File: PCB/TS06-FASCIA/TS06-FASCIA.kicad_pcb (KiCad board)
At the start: 2 copper layers, 176 x 52 mm, 18 parts, among them J1 PH 6, SW1 SR25 6-pos, SW2 FIELD, SW3 SUB, SW4 MINUS, SW5 PLUS

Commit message: Revert the fascia to placement + cosmetic gold; routing preserved on a branch
Board is back to what it was at 7213e72 in copper terms: footprints, nets, front
artwork and decorative gold, no functional traces. 0 segments, 0 vias.

Nothing is lost. Two ways back to the routed board:
  git checkout pcb/fascia-routed            the full routed board, audited clean
  tools/_fascia_routing.py.disabled         the block verbatim, paste it back

KEPT from the audit pass, because none of it is routing and all of it was wrong:
  mask openings inverted so gold has no bare-laminate halo
  SW1..SW5 designators off the product face, onto F.Fab
  dial leader lines horizontal instead of sloping away from their numerals
  MODE moved over the knob instead of stranded in the corner
  connector legend no longer printed on top of J1's designator

Also kept: J1's pin order as the routing chose it (D8, D7, GND, A7, +5V, A6). That
order puts each net on the pin nearest where it arrives from, which is worth having
whoever routes this next - it is not routing, it is a constraint the routing found.

tools/audit.py now recognises an unrouted board and says so once, rather than
reporting every net as split and burying the findings that matter.

Co-Authored-By: Claude Opus 5 <noreply@anthropic.com>
Claude-Session: https://claude.ai/code/session_01Wbajb7CU1SV8ZUPn3KkB8i
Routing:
- net GND: track 212.0 -> 0.00 mm
- net +5V: track 171.4 -> 0.00 mm, vias 3 -> 0
- net A6: track 99.1 -> 0.00 mm, vias 2 -> 0
- net A7: track 66.5 -> 0.00 mm
- net D8: track 15.6 -> 0.00 mm
- net D7: track 14.5 -> 0.00 mm
- net TAP5: track 9.97 -> 0.00 mm
- net TAP4: track 9.97 -> 0.00 mm
- net TAP3: track 9.97 -> 0.00 mm
- net TAP2: track 9.97 -> 0.00 mm
- net LEVB: track 5.02 -> 0.00 mm, vias 2 -> 0
- net LEVA: track 5.01 -> 0.00 mm

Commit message: PCB: TS06-FASCIA-THT, the through-hole variant, fully routed
A second build of the fascia in which the A6 divider is on show. Five axial
resistors sit on the face above the rotary's seven landing holes, and the copper
between them is bare - mask opened, ENIG gold, a solder fillet at every joint.
Everything else stays behind the panel with its front mask CLOSED, so the face
shows a drilled hole and no gold ring for those parts.

Routing: 34 tracks, no vias. The ladder is on F.Cu with the mask opened over it;
six signals run under mask on B.Cu; GND is a pour over the whole back face.

Two placement rules drove the layout and are written into the generator header:
a through-hole pad is copper on BOTH faces, so every back part must also miss the
decorative gold; and the panel parts have bodies behind the board, so R6-R8 live
in the strip below y 38.5, the only band clear of all five body keepouts.

J1's pin order is now a specification, not a routing convenience: 1 +5V, 2 GND,
3 A6, 4 A7, 5 D7, 6 D8, on BOTH builds. The old order was whatever the
surface-mount routing preferred; the through-hole board could not route to it,
and two variants of one product must not need two different cables. The
surface-mount board and the schematic are updated to match, and the shelved
routing block carries a caution that its five tails go to the old pins.

Toolchain, all of it prompted by faults found while building this board:
* tools/checkmatch.py - NEW. Compares the schematic netlist against the board
  pad by pad. Nothing did this before, which is how the two boards came to
  disagree about J1 in the first place.
* audit.py - rasterises a zone at 0.15 mm and flood-fills it, so "GND is poured"
  is a checked claim. Verified against a deliberate cut: it reports the split.
* checkpcb.py - now reads arcs and lettering on F.Cu as copper, not just lines.
  It found the plus and minus glyphs sitting 0.4 mm off the button landing pads.
* checkpcb.py, checkcopper.py - a non-greedy reach for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
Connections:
- J1 pad 1: D8 -> +5V
- J1 pad 2: D7 -> GND
- J1 pad 3: GND -> A6
- J1 pad 5: +5V -> D7
- J1 pad 6: A6 -> D8
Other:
- board text added: "1 +5V 2 GND 3 A6 4 A7 5 D7 6 D8"
- board text removed: "1 D8 2 D7 3 GND 4 A7 5 +5V 6 A6"
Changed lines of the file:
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@@
 		(size 1.0 3.5)
 		(layers "B.Cu" "B.Mask" "B.Paste")
-		(net 6 "D8")
+		(net 2 "+5V")
 		(roundrect_rratio 0.25)
 	)
@@
 		(size 1.0 3.5)
 		(layers "B.Cu" "B.Mask" "B.Paste")
-		(net 5 "D7")
+		(net 1 "GND")
 		(roundrect_rratio 0.25)
 	)
@@
 		(size 1.0 3.5)
 		(layers "B.Cu" "B.Mask" "B.Paste")
-		(net 1 "GND")
+		(net 3 "A6")
 		(roundrect_rratio 0.25)
 	)
@@
 		(size 1.0 3.5)
 		(layers "B.Cu" "B.Mask" "B.Paste")
-		(net 2 "+5V")
+		(net 5 "D7")
 		(roundrect_rratio 0.25)
 	)
@@
 		(size 1.0 3.5)
 		(layers "B.Cu" "B.Mask" "B.Paste")
-		(net 3 "A6")
+		(net 6 "D8")
 		(roundrect_rratio 0.25)
 	)
@@
 	(embedded_fonts no)
 )
-	(gr_text "1 D8  2 D7  3 GND  4 A7  5 +5V  6 A6"
+	(gr_text "1 +5V  2 GND  3 A6  4 A7  5 D7  6 D8"
 		(at 152.0 50.9 0)
 		(layer "B.SilkS")
@@
 		(generator_version "10.0")
 		(layer "F.Cu")
-		(at 4.5 4.5)
+	(at 4.5 4.5)
 		(descr "M2.5 clearance, non-plated")
 		(attr exclude_from_pos_files exclude_from_bom)
@@
 		(generator_version "10.0")
 		(layer "F.Cu")
-		(at 171.5 4.5)
+	(at 171.5 4.5)
 		(descr "M2.5 clearance, non-plated")
 		(attr exclude_from_pos_files exclude_from_bom)
@@
 		(generator_version "10.0")
 		(layer "F.Cu")
-		(at 4.5 47.5)
+	(at 4.5 47.5)
 		(descr "M2.5 clearance, non-plated")
 		(attr exclude_from_pos_files exclude_from_bom)
@@
 		(generator_version "10.0")
 		(layer "F.Cu")
-		(at 171.5 47.5)
+	(at 171.5 47.5)
 		(descr "M2.5 clearance, non-plated")
 		(attr exclude_from_pos_files exclude_from_bom)

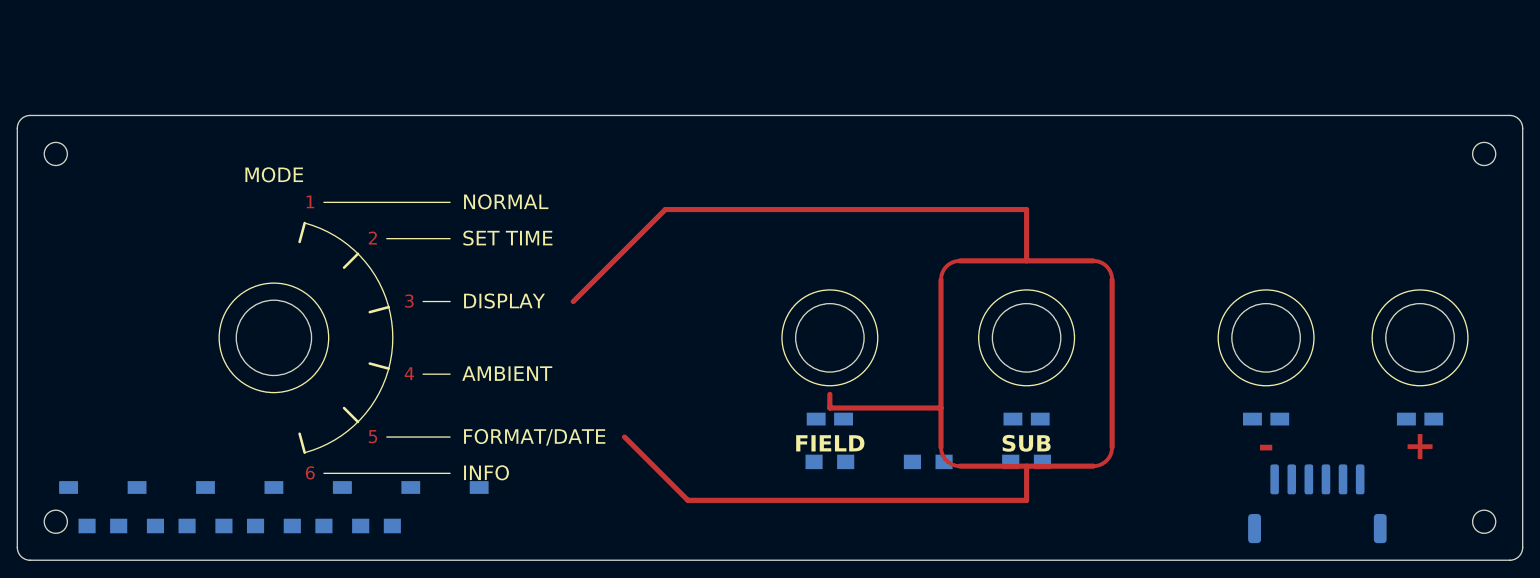
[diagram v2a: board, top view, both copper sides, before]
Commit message: PCB: TS06-FASCIA fully routed, zero vias anywhere on the board
The GND pour used to need two via-to-F.Cu bridges to reach three pads
(SW4.1, R8.2, R7.2) walled off by how densely the other five nets
packed into the R6/R7/R8 approach to J1. Relocating R6 out of that
corridor - the only placement change - opened enough room for the
pour to reach all seven GND pads on its own, confirmed against
KiCad's own computed filled_polygon data. 64 signal tracks, all on
B.Cu, no vias anywhere.

Also: checkpcb.py, checkcopper.py, checkmatch.py, audit.py and
render.py now parse .kicad_pcb files the way real KiCad actually
writes them (footprints indented normally rather than outdented to
column 0, every net reference - pads, tracks, vias, the zone itself -
written as a bare name with no code, and zone blocks that carry real
filled_polygon data rather than staying empty). Previously these
tools only understood this repo's own generator output; a real KiCad
save read as "0 footprints" or a falsely fragmented pour. Fixing the
parsers means board files never need reformatting by hand before a
check runs again.

J1's stale pre-fix pin-order description (symbol lib, both
schematics, and the mksch.py generator that produces them) is
corrected to match the real, fixed pin order.

Co-Authored-By: Claude Sonnet 5 <noreply@anthropic.com>
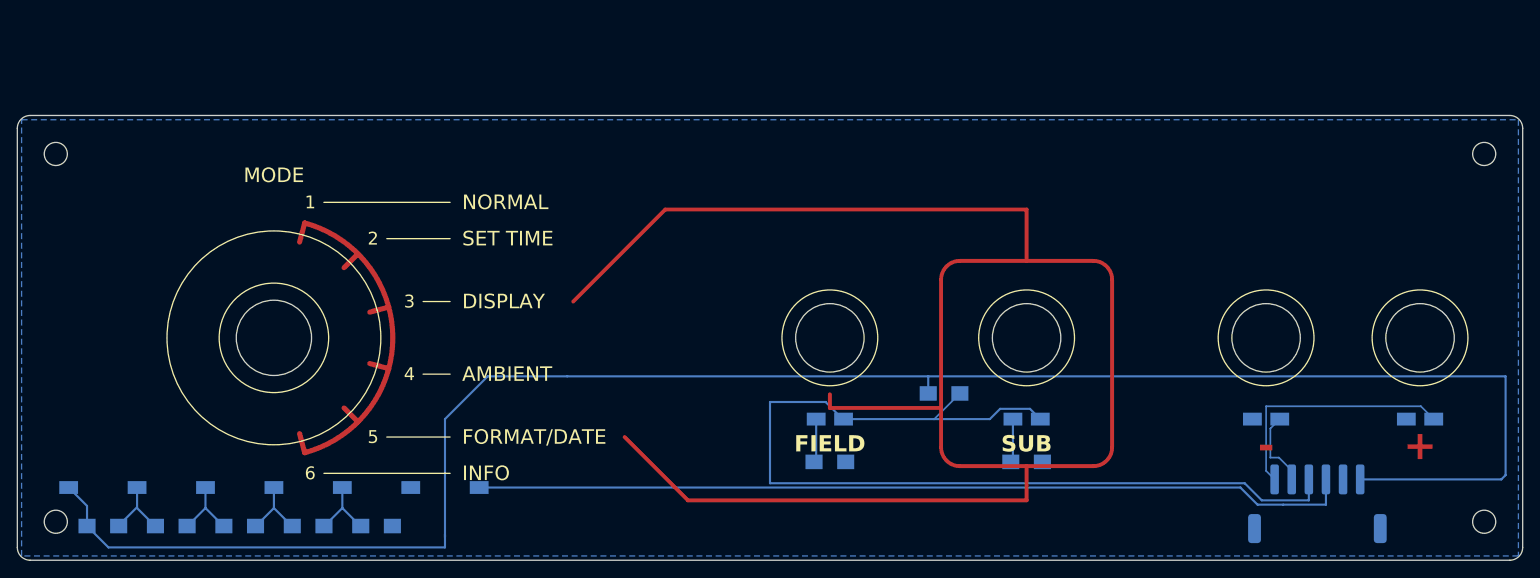
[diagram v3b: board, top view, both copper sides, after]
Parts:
- moved R6 8.21 mm to (108.3, 32.5)
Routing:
- net +5V: track 0.00 -> 220.4 mm
- net A7: track 0.00 -> 113.4 mm
- net A6: track 0.00 -> 102.8 mm
- net D8: track 0.00 -> 29.7 mm
- net D7: track 0.00 -> 9.73 mm
- net TAP5: track 0.00 -> 8.48 mm
- net TAP4: track 0.00 -> 8.34 mm
- net TAP3: track 0.00 -> 8.34 mm
- net TAP2: track 0.00 -> 8.34 mm
- net LEVB: track 0.00 -> 5.12 mm
- net LEVA: track 0.00 -> 5.12 mm
- added copper zone on B.Cu, net GND
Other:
- board text added: "1 D8 2 D7 3 GND 4 A7 5 +5V 6 A6"
- board text removed: "1 +5V 2 GND 3 A6 4 A7 5 D7 6 D8"

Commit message: PCB: fix stale J1 pin-order legend on the fascia back silkscreen
The physical silkscreen text still read the pre-fix order (D8, D7,
GND, A7, +5V, A6) even after the schematic/symbol description was
corrected earlier. THT's board and both mkpcb*.py generators already
had the right text - this was the one place it hadn't propagated to.

Co-Authored-By: Claude Sonnet 5 <noreply@anthropic.com>
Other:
- board text added: "1 +5V 2 GND 3 A6 4 A7 5 D7 6 D8"
- board text removed: "1 D8 2 D7 3 GND 4 A7 5 +5V 6 A6"
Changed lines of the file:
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@@
 		)
 	)
-	(gr_text "1 D8  2 D7  3 GND  4 A7  5 +5V  6 A6"
+	(gr_text "1 +5V  2 GND  3 A6  4 A7  5 D7  6 D8"
 		(at 152 50.9 0)
 		(layer "B.SilkS")

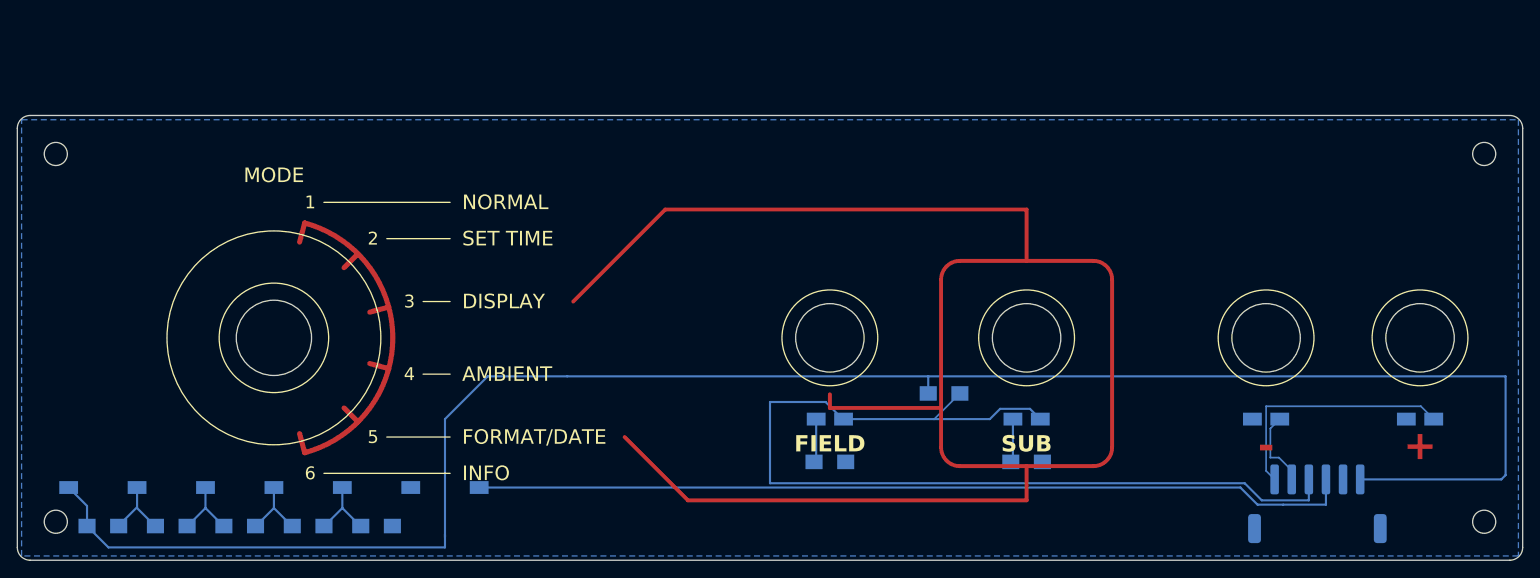
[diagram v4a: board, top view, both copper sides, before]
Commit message: PCB: TS06-SEC routed, checker fixes, 3D assembly and the TS06-MAIN brief
Work left uncommitted by the session that drew TS06-SEC, committed as-is so the
TS06-MAIN work that follows starts from a clean tree:

- PCB/TS06-SEC: surface-mount build, placed and routed by tools/mkpcb_sec.py
  with the new grid router tools/pcbroute.py (negotiated routing, HV clearance class)
- tools/mkfp_sec.py and the pre-rotated back-side footprints it generates;
  corrected TS06_IN12_Socket / TS06_IN17_Socket (Y mirror, anode pad, no pip hole)
- audit.py, checkcopper.py, checkpcb.py, render.py fixes (both KiCad file dialects)
- TS06-FASCIA compressed to 40 mm; PCB/README.md updated
- 3d/Clock.FCStd reviewed 8-tube assembly, IN17 model, STEP exports,
  PCB/IN-12_norm/gyver.kicad_pcb (gerbview import of the inherited board)
- knowledge/ snapshot of the project documents; render/rev_f.py
- Claude outputs/TS06-MAIN-handoff.md, the brief for the combined main board

Co-Authored-By: Claude Fable 5.1 <noreply@anthropic.com>
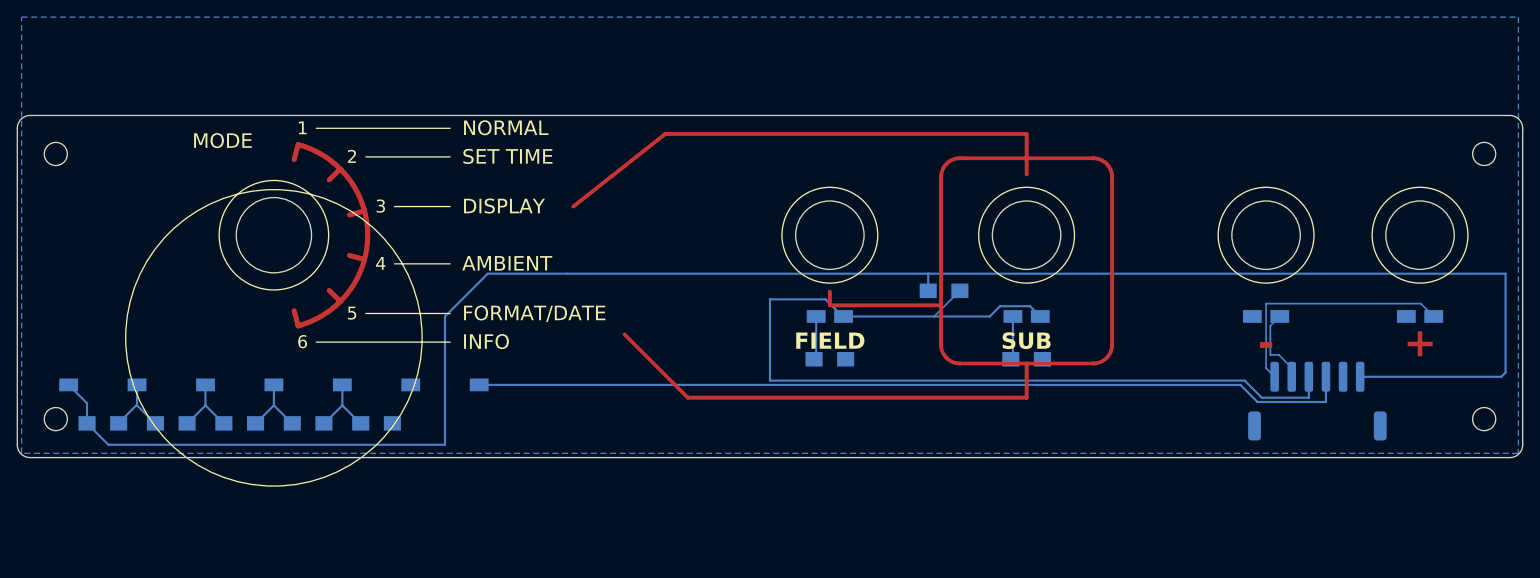
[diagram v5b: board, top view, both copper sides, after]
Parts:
- moved ? 12.0 mm to (171.5, 35.5)
- moved ? 12.0 mm to (4.50, 35.5)
- moved J1 12.0 mm to (152.0, 33.4)
- moved R1 12.0 mm to (42.0, 36.0)
- moved R2 12.0 mm to (34.0, 36.0)
- moved R3 12.0 mm to (26.0, 36.0)
- moved R4 12.0 mm to (18.0, 36.0)
- moved R5 12.0 mm to (10.0, 36.0)
- moved R6 12.0 mm to (108.3, 20.5)
- moved R7 12.0 mm to (95.0, 28.5)
- moved R8 12.0 mm to (118.0, 28.5)
- moved SW1 12.0 mm to (30.0, 14.0)
- moved SW2 12.0 mm to (95.0, 14.0)
- moved SW3 12.0 mm to (118.0, 14.0)
- moved SW4 12.0 mm to (146.0, 14.0)
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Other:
- board size 176 x 52 mm -> 176 x 40 mm
